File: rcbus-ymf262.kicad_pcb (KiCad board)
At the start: 2 copper layers, 100 x 50 mm, 42 parts, among them CON1 SJ1-3523N, P1 RC2014 BUS, U1 74HCT688, U2 YMF262, U3 YAC512, U4 TL074, X1 14.318MHz

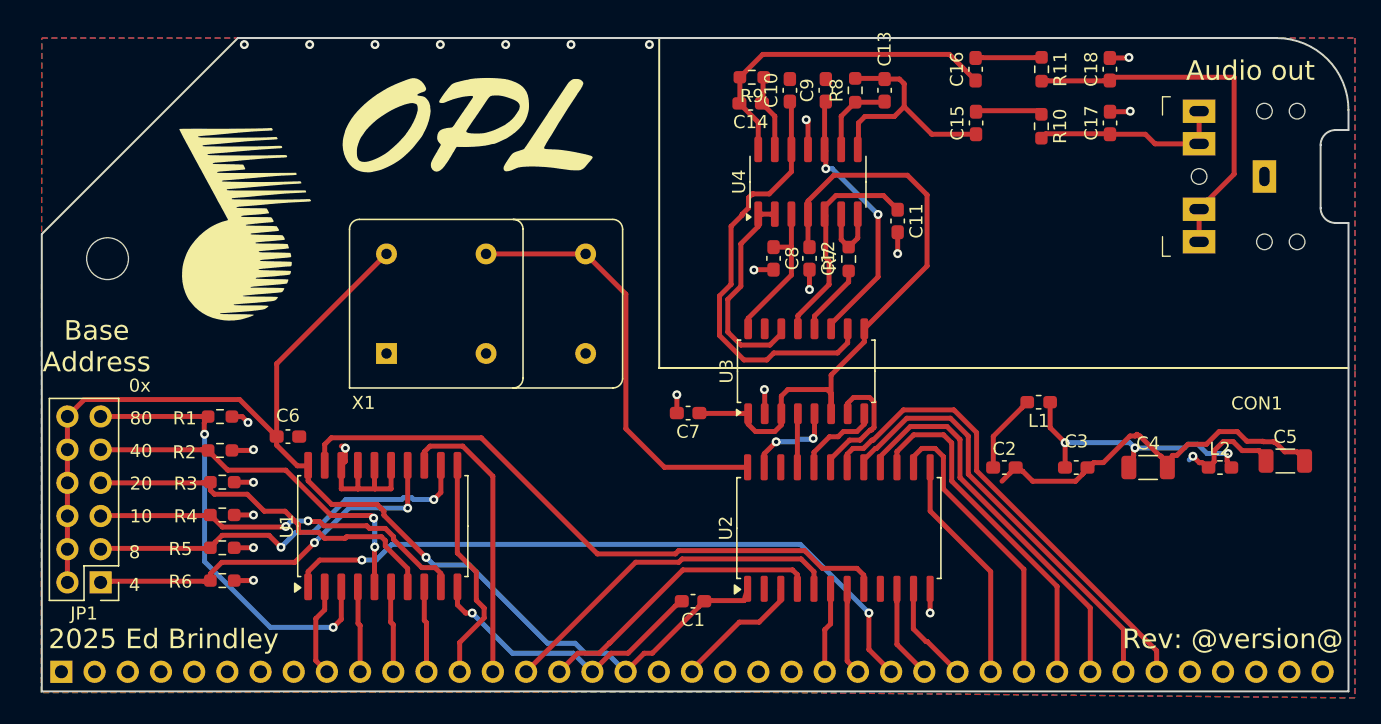
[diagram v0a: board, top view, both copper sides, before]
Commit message: use smd oscillator
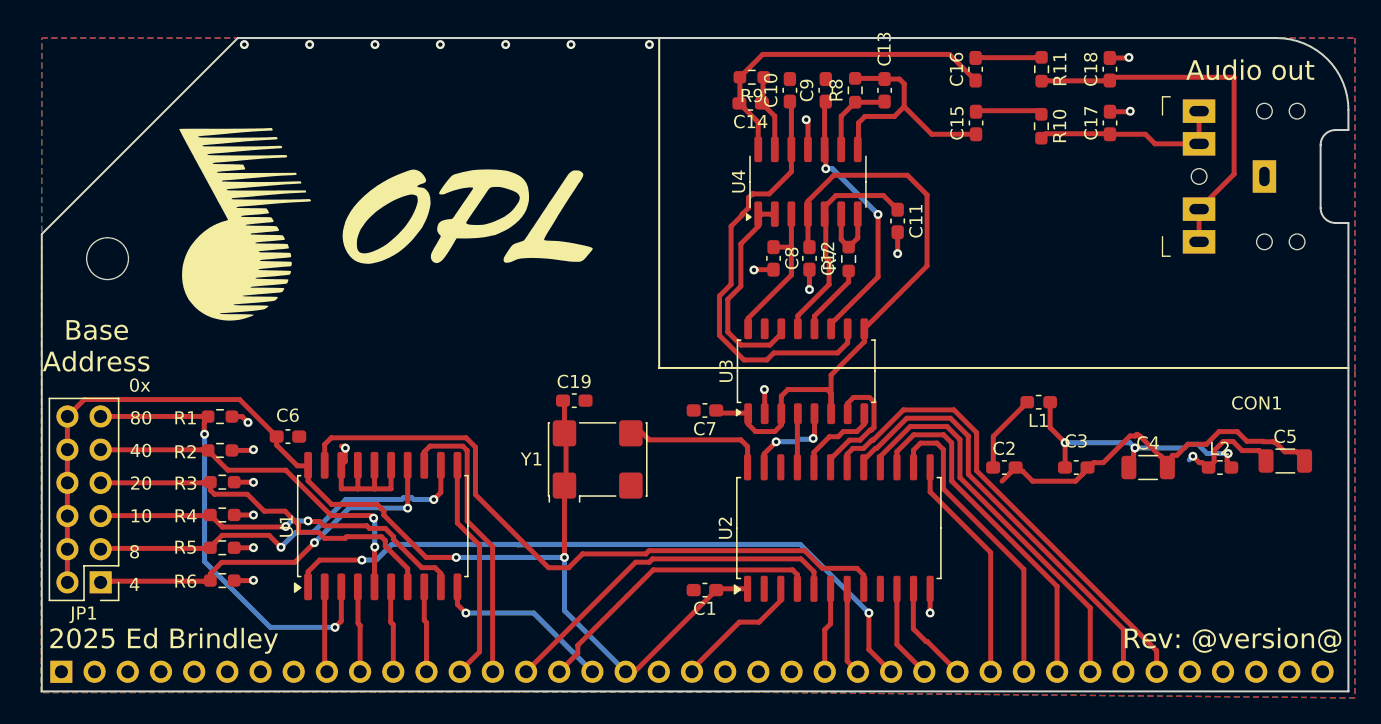
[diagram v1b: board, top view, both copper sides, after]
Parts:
- removed X1: 14.318MHz, electrified:Oscillator_DIP-8-14
- added C19: 0.1uF, Capacitor_SMD:C_0603_1608Metric_Pad1.08x0.95mm_HandSolder, F.Cu at (101.2, 142.2)
- added Y1: SG-8002CA, Oscillator:Oscillator_SMD_Abracon_ASV-4Pin_7.0x5.1mm, F.Cu at (103.0, 146.8)
- moved G2 7.00 mm to (93.0, 128.0)
- moved C7 1.30 mm to (111.2, 143.0)
- moved C1 1.25 mm to (111.2, 156.8)
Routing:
- net /CLK: track 32.8 -> 10.9 mm
- net GND: track 79.5 -> 69.0 mm, vias 18 -> 17
- net /~{CS}: track 48.7 -> 51.7 mm
- net VCC: track 101.6 -> 98.9 mm, vias 1 -> 2
- net /D3: track 22.6 -> 23.6 mm
- net +5VA: track 57.3 -> 56.5 mm
- net /A7: track 7.13 -> 6.57 mm

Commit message: set version no
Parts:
- moved C6 0.66 mm to (80.0, 145.0), turned to 180 degrees
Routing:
- net VCC: track 98.9 -> 101.7 mm
- net GND: vias 17 -> 67

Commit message: more versioning stuff
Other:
- board text added: "Rev: ${VERSION} ${GIT_HASH}"
- board text removed: "Rev: @version@"

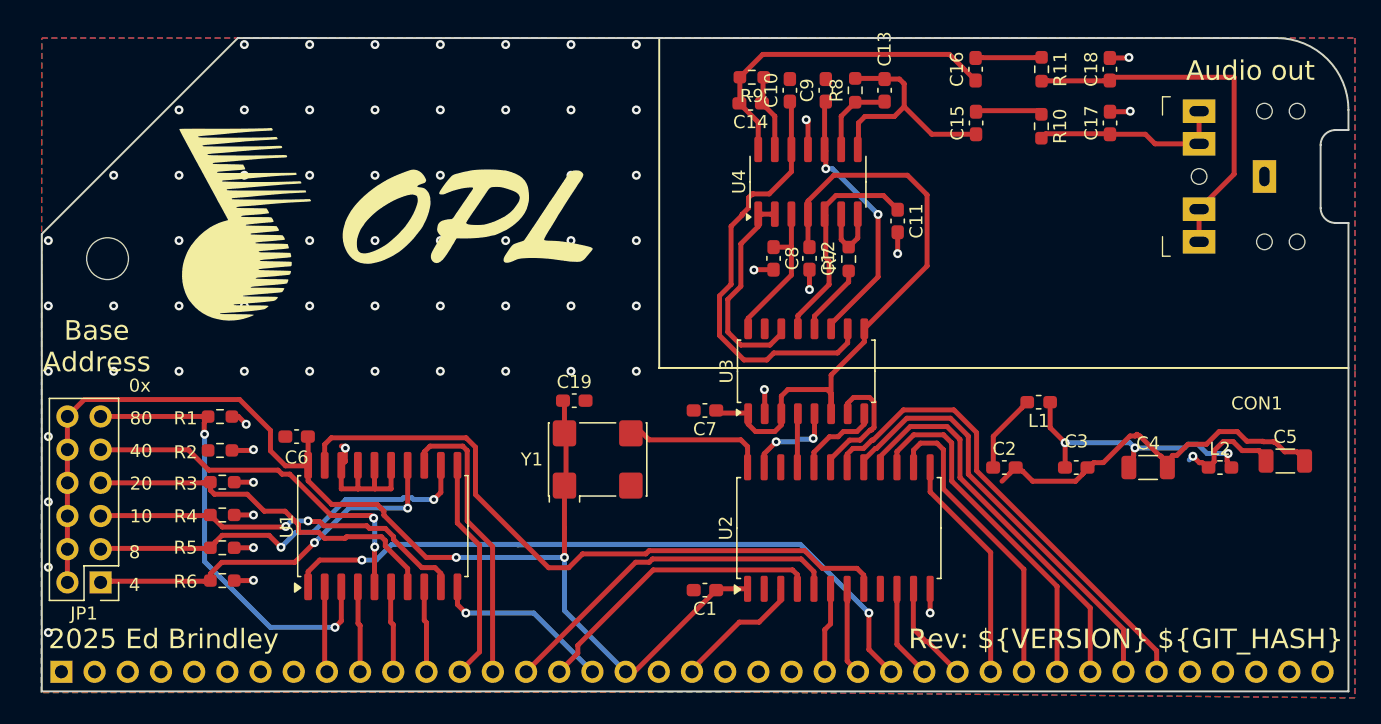
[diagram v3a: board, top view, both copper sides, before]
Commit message: remove gnda, another attempt at versioning
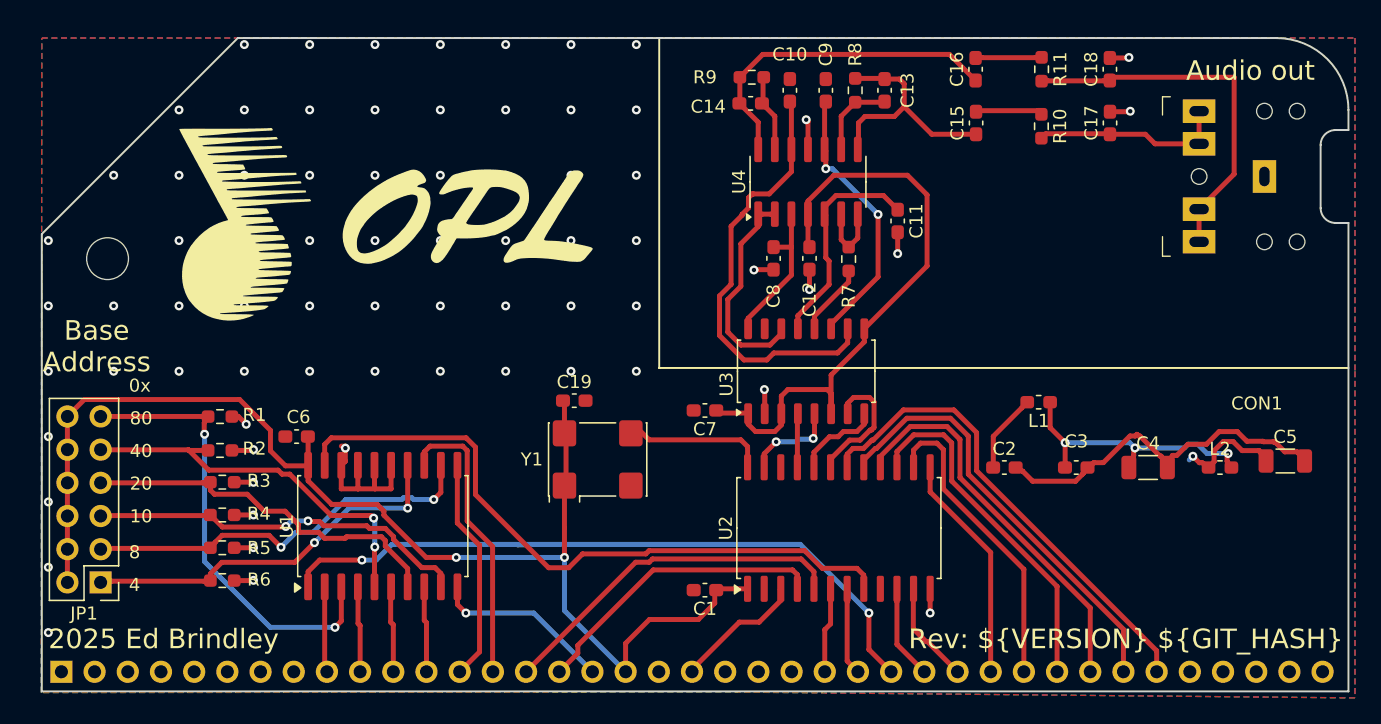
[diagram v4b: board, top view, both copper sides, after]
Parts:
- turned R1 to 0 degrees
- turned R2 to 0 degrees
- turned R3 to 0 degrees
- turned R4 to 0 degrees
- turned R5 to 0 degrees
- turned R6 to 0 degrees
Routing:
- net GND: track 69.0 -> 76.5 mm, vias 67 -> 73
- net VCC: track 101.7 -> 103.5 mm
- net Net-(JP1-Pin_1): track 30.2 -> 28.7 mm, vias 3 -> 2
- net Net-(JP1-Pin_3): track 32.3 -> 30.8 mm, vias 3 -> 2
- net Net-(JP1-Pin_7): track 29.5 -> 28.1 mm, vias 1 -> 0
- net Net-(JP1-Pin_5): track 30.9 -> 29.4 mm, vias 3 -> 2
- net Net-(JP1-Pin_11): track 35.8 -> 34.5 mm, vias 3 -> 2
- net Net-(JP1-Pin_9): track 30.0 -> 29.9 mm, vias 3 -> 2

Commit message: more kibot work
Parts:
- moved C2 53.7 mm to (81.5, 137.0)
- moved C3 53.7 mm to (87.0, 137.0)
- moved C4 53.7 mm to (92.5, 137.0)
- moved C5 53.7 mm to (103.0, 136.5)
- moved L1 53.7 mm to (84.1, 132.0)
- moved L2 53.7 mm to (98.0, 137.0)
- moved G2 2.00 mm to (93.0, 126.0)
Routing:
- net VCC: track 103.5 -> 129.8 mm
- net +5VA: track 56.5 -> 69.8 mm
- net GND: track 76.5 -> 64.6 mm, vias 73 -> 62
- net /D7: track 37.0 -> 41.7 mm
- net /D6: track 33.4 -> 36.1 mm
- net /D5: track 30.2 -> 31.6 mm
- net Net-(JP1-Pin_9): track 29.9 -> 30.5 mm

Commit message: reorg
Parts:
- moved C16 9.41 mm to (132.0, 126.3)
- moved C18 9.41 mm to (142.3, 126.3)
- moved R11 9.41 mm to (137.1, 126.3)
- moved C5 6.84 mm to (96.2, 137.2), turned to 90 degrees
- moved C11 5.33 mm to (121.5, 131.4)
- moved L1 5.14 mm to (84.5, 137.1), turned to -90 degrees
- moved L2 5.00 mm to (93.0, 137.1), turned to 90 degrees
- moved C4 2.51 mm to (90.0, 137.2), turned to -90 degrees
- moved R7 1.00 mm to (123.2, 131.4)
- moved C2 0.51 mm to (82.0, 137.1), turned to 90 degrees
- moved C3 0.11 mm to (87.0, 137.1), turned to -90 degrees
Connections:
- C10 pad 1: /AUDIO_CH1 -> /AUDIO_CH2
- C13 pad 1: /L -> /R
- C14 pad 2: /R -> /L
- C9 pad 1: /AUDIO_CH2 -> /AUDIO_CH1
- R8 pad 2: /L -> /R
- R9 pad 2: /R -> /L
- U4 pad 10: /AUDIO_CH2 -> /AUDIO_CH1
- U4 pad 12: /AUDIO_CH1 -> /AUDIO_CH2
- U4 pad 14: /R -> /L
- U4 pad 8: /L -> /R
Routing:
- net GND: track 64.6 -> 34.7 mm
- net Net-(C18-Pad1): track 28.0 -> 14.5 mm
- net Net-(C3-Pad1): track 21.1 -> 8.93 mm, vias 3 -> 0
- net /L: track 18.1 -> 29.7 mm
- net /AUDIO_CH1: track 33.2 -> 22.7 mm
- net VCC: track 129.8 -> 125.3 mm
- net Net-(U3-AOUT): track 16.9 -> 12.6 mm
- net /AUDIO_CH2: track 20.9 -> 23.6 mm, vias 2 -> 0
- net /R: track 25.7 -> 23.0 mm
- net Net-(U4B--): track 5.58 -> 3.92 mm
- net Net-(JP1-Pin_1): track 28.7 -> 29.5 mm
- net +5VA: track 69.8 -> 70.4 mm, vias 1 -> 0
- net Net-(U3-SWIN): track 5.51 -> 6.14 mm
- net /~{CS}: track 51.7 -> 52.2 mm
- net Net-(JP1-Pin_7): track 28.1 -> 27.6 mm

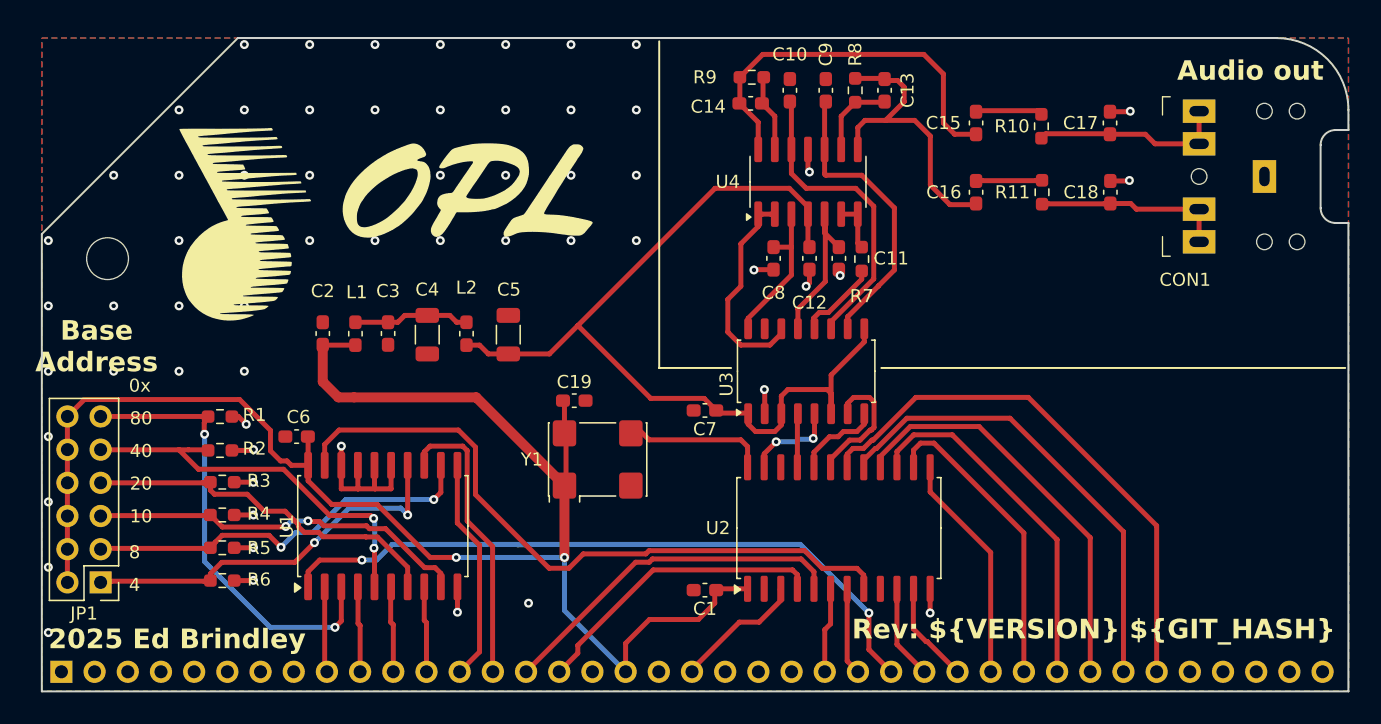
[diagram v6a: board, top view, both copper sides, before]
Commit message: some pcb tidyup, use netcallses for track widths
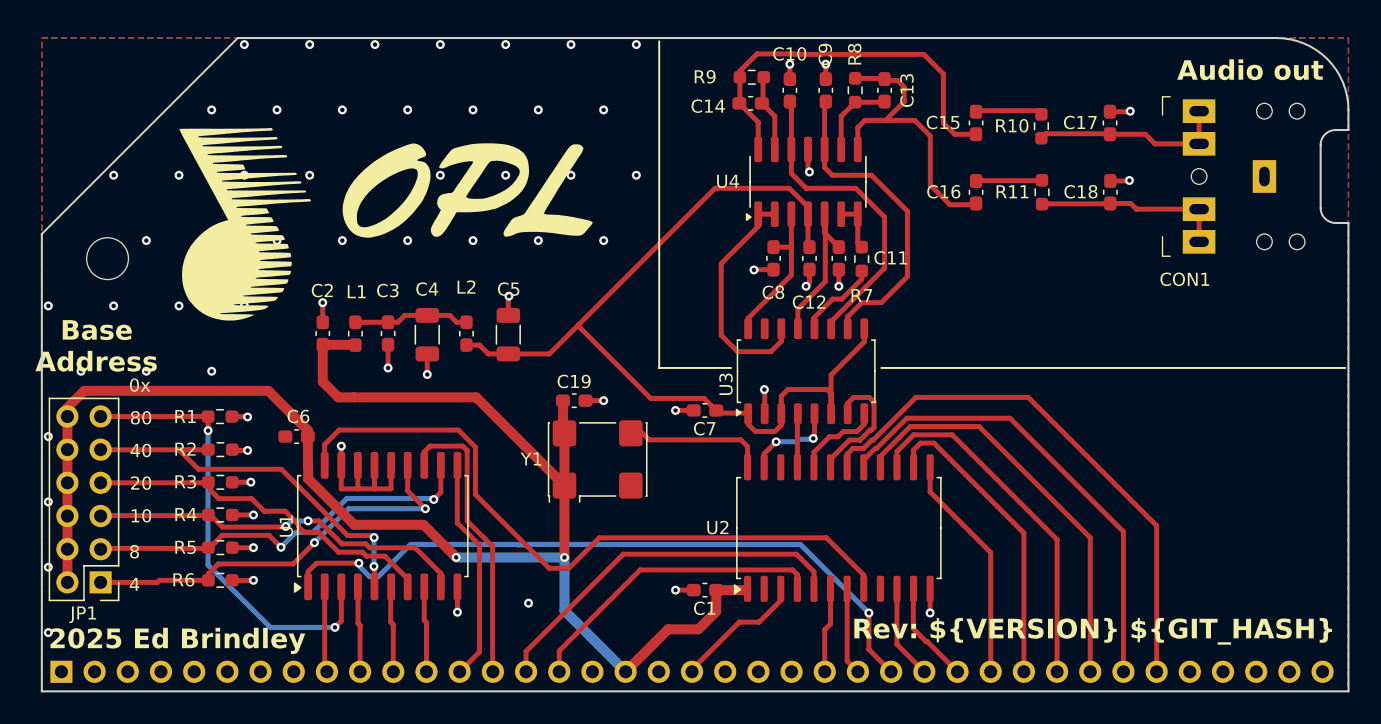
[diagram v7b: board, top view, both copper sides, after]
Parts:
- moved R6 0.15 mm to (74.2, 156.0)
- moved R3 0.15 mm to (74.2, 148.5)
- moved R5 0.15 mm to (74.2, 153.5)
- moved R4 0.15 mm to (74.2, 151.0)
- moved R2 0.06 mm to (74.2, 146.0)
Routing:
- net GND: track 34.7 -> 47.5 mm, vias 62 -> 68
- net VCC: track 125.3 -> 122.2 mm
- net Net-(JP1-Pin_1): track 29.5 -> 31.4 mm
- net /AUDIO_CH1: track 22.7 -> 24.6 mm
- net Net-(U3-MP): track 16.3 -> 17.9 mm
- net /A1: track 27.3 -> 28.5 mm
- net /~{IORQ}: track 52.4 -> 53.3 mm
- net Net-(JP1-Pin_9): track 30.6 -> 29.7 mm
- net /~{CS}: track 52.2 -> 53.0 mm
- net /AUDIO_CH2: track 23.6 -> 24.3 mm
- net /A0: track 23.0 -> 23.6 mm
- net Net-(JP1-Pin_7): track 27.6 -> 27.0 mm

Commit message: update logo
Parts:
- moved G2 4.98 mm to (94.5, 121.2)
- moved C15 4.75 mm to (136.8, 121.0)
- moved C16 4.75 mm to (136.8, 126.3)
- moved G1 4.30 mm to (78.0, 125.0)
- moved R10 2.51 mm to (139.5, 121.0)
- moved R11 2.45 mm to (139.5, 126.3)
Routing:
- net /R: track 23.0 -> 27.7 mm
- net Net-(C17-Pad1): track 15.0 -> 12.4 mm
- net /L: track 30.0 -> 32.6 mm
- net Net-(C15-Pad2): track 5.15 -> 2.77 mm
- net Net-(C18-Pad1): track 14.5 -> 12.6 mm
- net Net-(C16-Pad2): track 4.48 -> 2.77 mm
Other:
- board text added: "RCBus OPL3 Sound Card"
